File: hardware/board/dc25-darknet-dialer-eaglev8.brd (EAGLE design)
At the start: 101.6 x 101.6 mm, 83 parts, among them SW1 RESET, X1 USB-MICROB, Y1 RESONATORSMD

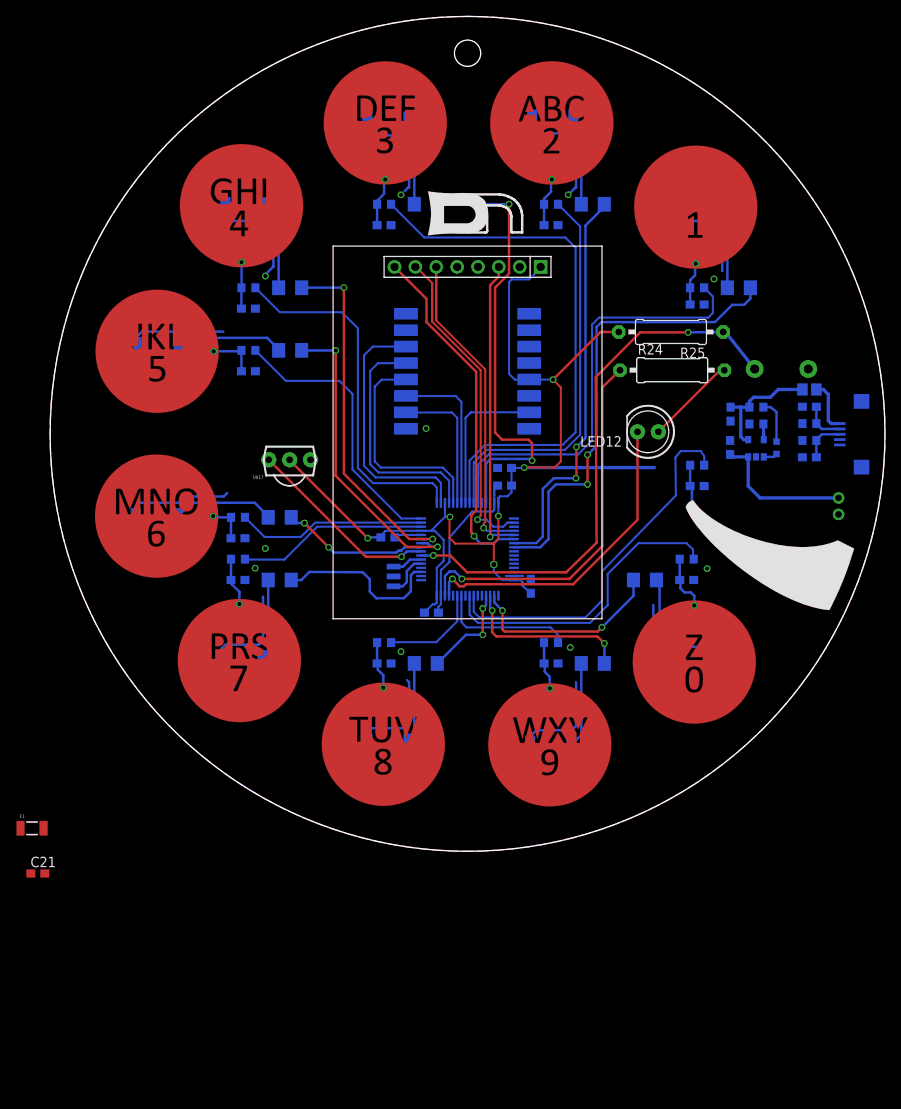
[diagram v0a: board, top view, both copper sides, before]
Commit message: added stlink connector to lbr moved radio spi from spi1 to spi3 to free up pins for touch sensening
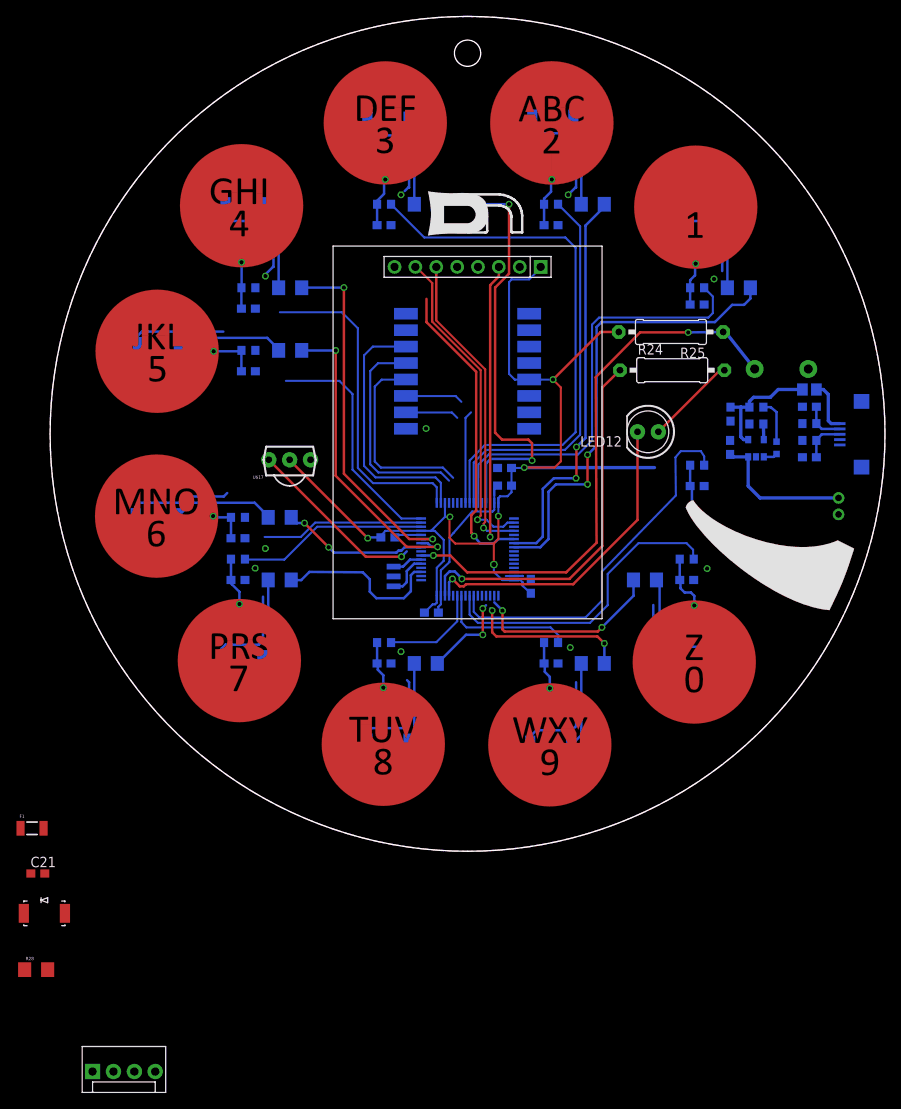
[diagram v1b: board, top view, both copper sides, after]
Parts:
- added LED13: (no value), SYNShop:GULLWING_LED
- added R28: (no value), SYNShop:1206
- added STLINK: STLINK-V2-CONNECTOR, darknet_parts_library:1X04
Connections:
- net N$43 renamed TIM_IR_CARRIER_FREQ
- removed net N$44: U$2.P54
- removed net N$45: U$2.P53
- removed net N$46: U$2.P43
- removed net N$48: U$2.P42
- removed net N$61: U$2.P30
- removed net N$66: U$12.A0
- removed net N$67: U$12.RESET
- removed net OLED_LED: U$12.LED, U$2.P38
- removed net OLED_SPI_MISO: U$2.P35
- new net N$29: LED13.A, R28.2
- new net N$50: U$2.P23
- new net OLED_BACK_LIT: U$12.LED, U$2.P37
- new net OLED_DATA_CMD: U$12.A0, U$2.P35
- new net OLED_RESET: U$12.RESET, U$2.P38
- new net RMF69_INTERRUPT_DIO1: U$15.DIO1, U$2.P30
- new net TSC_G2_I01: R18.1, U$2.P20
- new net TSC_G2_I02: R17.1, U$2.P21
- new net TSC__G2_I03: U$2.P22
- net GND: now also LED13.C, STLINK.GND
- net IR_RCV: now also U$2.P54; no longer U$2.P8
- net LED10: now also U$2.P43; no longer U$2.P50
- net LED8: now also U$2.P8; no longer U$2.P52
- net LED9: now also U$2.P42; no longer U$2.P51
- net LED_STATUS: now also R28.1
- net OLED_CS: no longer U$2.P37
- net RFM69_SPI_MISO: now also U$2.P52; no longer U$2.P22
- net RFM69_SPI_MOSI: now also U$2.P53; no longer U$2.P23
- net RFM69_SPI_NSS: now also U$2.P50; no longer U$2.P20
- net RFM69_SPI_SCK: now also U$2.P51; no longer U$2.P21
- net RMF69_INTERRUPT_DIO0: now also U$15.DIO0; no longer U$15.DIO1
- net SYS_JTCK-SWCLK: now also STLINK.SWDCLK
- net SYS_JTMS_SWDIO: now also STLINK.SWDIO
- net TSC_G1_IO1: now also R16.1; no longer R17.1
- net TSC_G1_IO2: now also R15.1; no longer R16.1
- net TSC_G1_IO3: now also R14.1; no longer R15.1
- net TSC_G1_IO4: no longer R14.1
- net TSC_G5_IO4: no longer R18.1
- net VCC: now also STLINK.VCC
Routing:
- net OLED_LED: track 42.8 -> 0.00 mm, vias 1 -> 0
- net OLED_RESET: track 0.00 -> 37.3 mm, vias 0 -> 1
- net RFM69_SPI_MOSI: track 19.3 -> 7.05 mm
- net RFM69_SPI_MISO: track 16.9 -> 6.53 mm
- net RMF69_INTERRUPT_DIO0: track 18.4 -> 11.3 mm
- net TSC_G1_IO3: track 34.0 -> 28.8 mm
- net TSC_G1_IO4: track 44.0 -> 39.8 mm
- net TSC_G1_IO2: track 23.2 -> 19.8 mm
- net RFM69_SPI_SCK: track 26.7 -> 23.6 mm
- net RFM69_SPI_NSS: track 29.2 -> 26.5 mm
- net OLED_CS: track 36.3 -> 33.6 mm
- net IR_RCV: track 23.7 -> 21.9 mm
- net LED9: track 21.2 -> 19.7 mm
- net LED8: track 11.9 -> 10.7 mm
- net LED10: track 24.3 -> 23.5 mm

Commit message: moved parts onto board, but not in correct location yet
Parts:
- moved STLINK 127.2 mm to (92.3, 70.4), turned to 89.3 degrees
- moved F1 94.9 mm to (84.5, 41.4)
- moved R28 55.5 mm to (31.4, 30.1)
- moved LED13 48.7 mm to (32.4, 27.2)
- moved C21 43.2 mm to (33.9, 22.1)
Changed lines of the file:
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@@
 <element name="L1" library="dp_devices" package="FB603" value="" x="92.4" y="56.2" rot="MR180"/>
 <element name="Y1" library="SparkFun" package="RESONATOR-SMD" value="RESONATORSMD" x="41.8" y="33.45" rot="MR90"/>
-<element name="F1" library="SparkFun" package="PTC-1206" value="500uA" x="-2.2" y="2.8"/>
-<element name="C21" library="SYNShop" package="C0603" value="" x="-1.5" y="-2.7"/>
-<element name="LED13" library="SYNShop" package="GULLWING_LED" value="" x="-3.2" y="-6.05"/>
-<element name="R28" library="SYNShop" package="1206" value="" x="-1.7" y="-14.4"/>
-<element name="STLINK" library="darknet_parts_library" package="1X04" value="STLINK-V2-CONNECTOR" x="10.25" y="-26.8"/>
+<element name="F1" library="SparkFun" package="PTC-1206" value="500uA" x="84.45" y="41.4"/>
+<element name="C21" library="SYNShop" package="C0603" value="" x="33.9" y="22.05"/>
+<element name="LED13" library="SYNShop" package="GULLWING_LED" value="" x="32.4" y="27.2"/>
+<element name="R28" library="SYNShop" package="1206" value="" x="31.4" y="30.15"/>
+<element name="STLINK" library="darknet_parts_library" package="1X04" value="STLINK-V2-CONNECTOR" x="92.35" y="70.4" rot="R89.3"/>
 </elements>
 <signals>
@@
 <wire x1="42.7" y1="79.9" x2="41.49" y2="76.2" width="0" layer="19" extent="16-16"/>
 <wire x1="43.15" y1="80.35" x2="42.7" y2="79.9" width="0" layer="19" extent="16-16"/>
-<wire x1="-2.35" y1="-2.7" x2="20.828" y2="23.344" width="0" layer="19" extent="1-16"/>
-<wire x1="-3.2" y1="-7.55" x2="-2.35" y2="-2.7" width="0" layer="19" extent="1-1"/>
-<wire x1="12.79" y1="-26.8" x2="-3.2" y2="-7.55" width="0" layer="19" extent="1-1"/>
+<wire x1="33.05" y1="22.05" x2="20.828" y2="23.344" width="0" layer="19" extent="1-16"/>
+<wire x1="32.4" y1="25.7" x2="33.05" y2="22.05" width="0" layer="19" extent="1-1"/>
+<wire x1="92.381028125" y1="72.939809375" x2="32.4" y2="25.7" width="0" layer="19" extent="1-1"/>
 </signal>
 <signal name="N$1">
@@
 <contactref element="U$2" pad="P46"/>
 <contactref element="STLINK" pad="SWDIO"/>
-<wire x1="7.71" y1="-26.8" x2="56.45" y2="34" width="0" layer="19" extent="16-16"/>
+<wire x1="92.31896875" y1="67.8601875" x2="56.45" y2="34" width="0" layer="19" extent="16-16"/>
 </signal>
 <signal name="SYS_JTCK-SWCLK">
 <contactref element="U$2" pad="P49"/>
 <contactref element="STLINK" pad="SWDCLK"/>
-<wire x1="10.25" y1="-26.8" x2="54.55" y2="31.1" width="0" layer="19" extent="16-16"/>
+<wire x1="92.35" y1="70.4" x2="54.55" y2="31.1" width="0" layer="19" extent="16-16"/>
 </signal>
 <signal name="TSC_G5_IO1">
@@
 <contactref element="C21" pad="2"/>
 <contactref element="STLINK" pad="VCC"/>
-<wire x1="-0.65" y1="-2.7" x2="45.55" y2="29.05" width="0" layer="19" extent="1-16"/>
-<wire x1="5.17" y1="-26.8" x2="-0.65" y2="-2.7" width="0" layer="19" extent="1-1"/>
+<wire x1="34.75" y1="22.05" x2="45.55" y2="29.05" width="0" layer="19" extent="1-16"/>
+<wire x1="92.2879375" y1="65.320378125" x2="34.75" y2="22.05" width="0" layer="19" extent="1-1"/>
 </signal>
 <signal name="TSC_G3_IO2">
@@
 <contactref element="U$2" pad="P2"/>
 <contactref element="R28" pad="1"/>
-<wire x1="-3.1" y1="-14.4" x2="45.15" y2="33.5" width="0" layer="19" extent="1-16"/>
+<wire x1="30" y1="30.15" x2="45.15" y2="33.5" width="0" layer="19" extent="1-16"/>
 </signal>
 <signal name="TIM_IR_MAIN_SIGNAL">
@@
 <wire x1="84.95" y1="44.45" x2="84.95" y2="48" width="0.4064" layer="16"/>
 <contactref element="F1" pad="1"/>
-<wire x1="-3.6" y1="2.8" x2="82.75" y2="48.3" width="0" layer="19" extent="1-16"/>
+<wire x1="83.05" y1="41.4" x2="82.75" y2="48.3" width="0" layer="19" extent="1-16"/>
 </signal>
 <signal name="N$31">
@@
 <contactref element="LED13" pad="A"/>
 <contactref element="R28" pad="2"/>
-<wire x1="1.8" y1="-7.55" x2="-0.3" y2="-14.4" width="0" layer="19" extent="1-1"/>
+<wire x1="37.4" y1="25.7" x2="32.8" y2="30.15" width="0" layer="19" extent="1-1"/>
 </signal>
 <signal name="TSC_G2_I01">

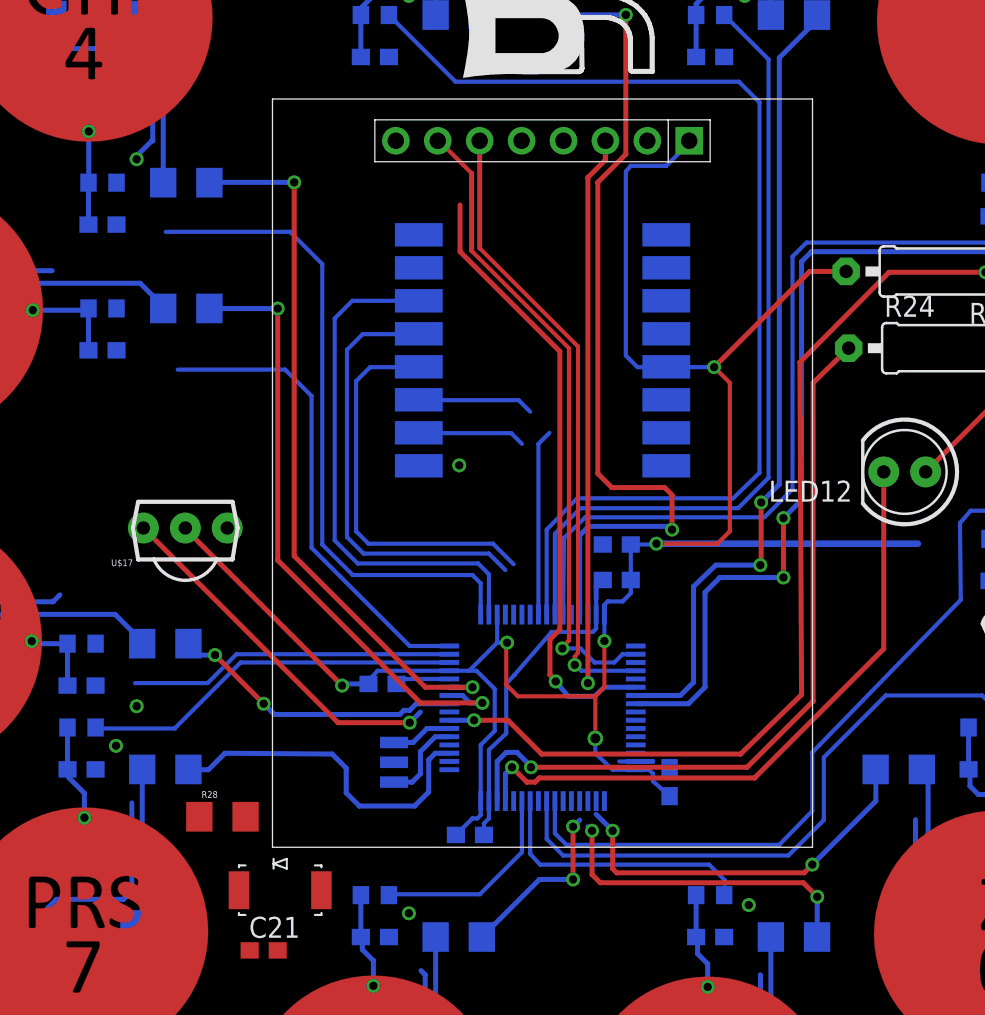
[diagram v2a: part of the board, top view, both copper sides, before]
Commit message: updates to only have 1 pin for IR timer added todo list
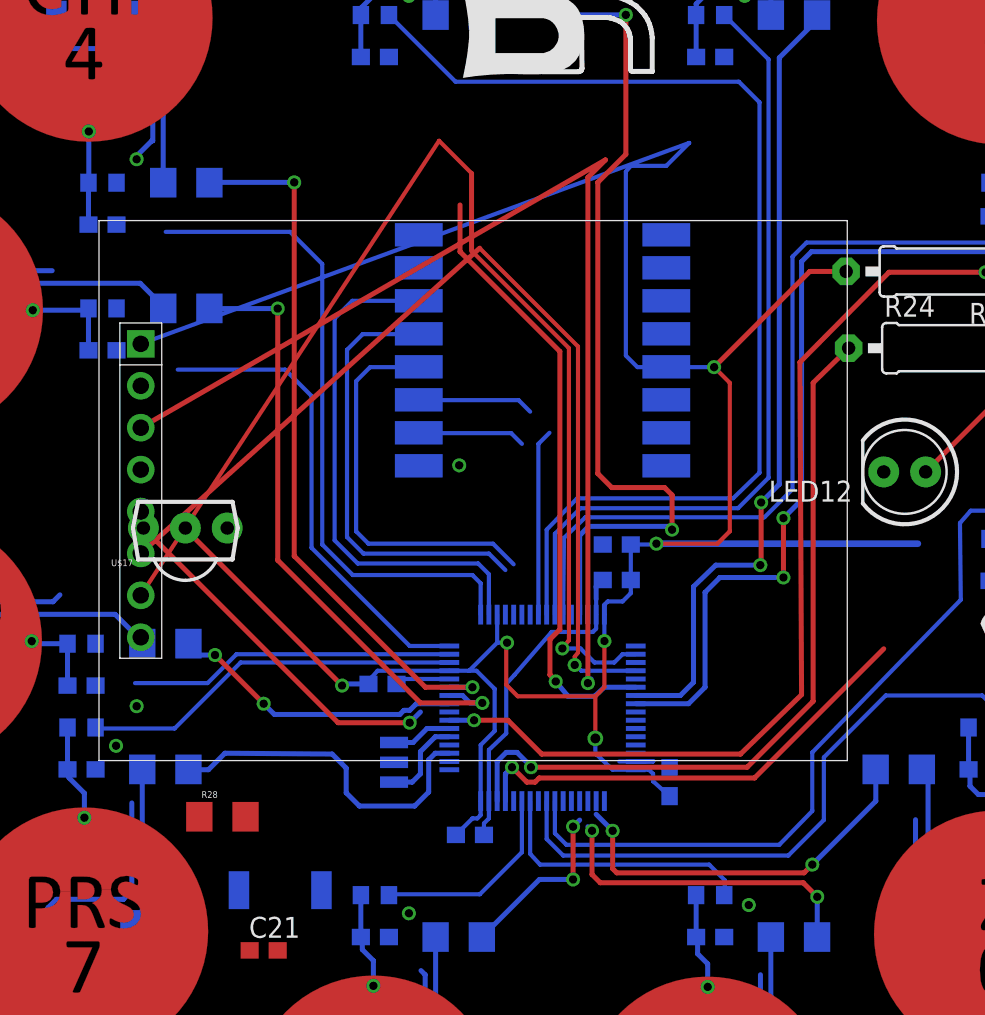
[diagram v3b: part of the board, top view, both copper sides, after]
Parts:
- moved U$12 32.3 mm to (26.4, 49.9), turned to 90 degrees
- moved LED13 5.00 mm to (37.4, 27.2), flipped to the bottom
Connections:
- removed net TIM_IR_MAIN_SIGNAL: LED12.K, U$2.P61
- new net SD_CARD_CS: U$2.P57
- net TIM_IR_CARRIER_FREQ: now also LED12.K, U$2.P61; no longer U$2.P57
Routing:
- net TIM_IR_MAIN_SIGNAL: track 39.2 -> 0.00 mm, vias 1 -> 0
- net VCC: track 130.9 -> 166.2 mm
- net OLED_SPI_SCK: track 39.3 -> 72.1 mm
- net OLED_CS: track 33.6 -> 65.0 mm
- net TIM_IR_CARRIER_FREQ: track 0.00 -> 28.5 mm, vias 0 -> 1
- net OLED_SPI_MOSI: track 38.2 -> 59.3 mm

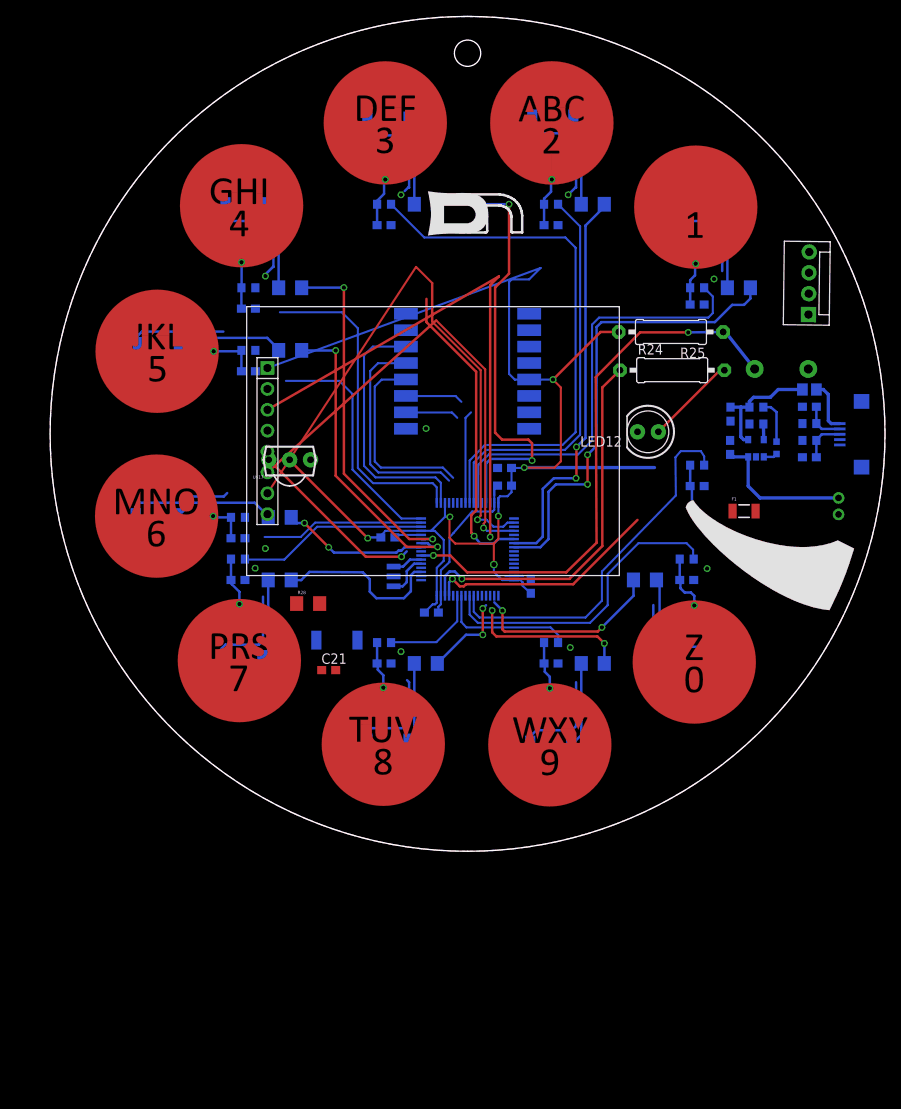
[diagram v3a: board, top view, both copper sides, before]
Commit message: added new part to library: SD_CARD_HEADER diff of todo.txt shows what else was completed on this check in. adding another doc on cap sense and updated stm32cube file
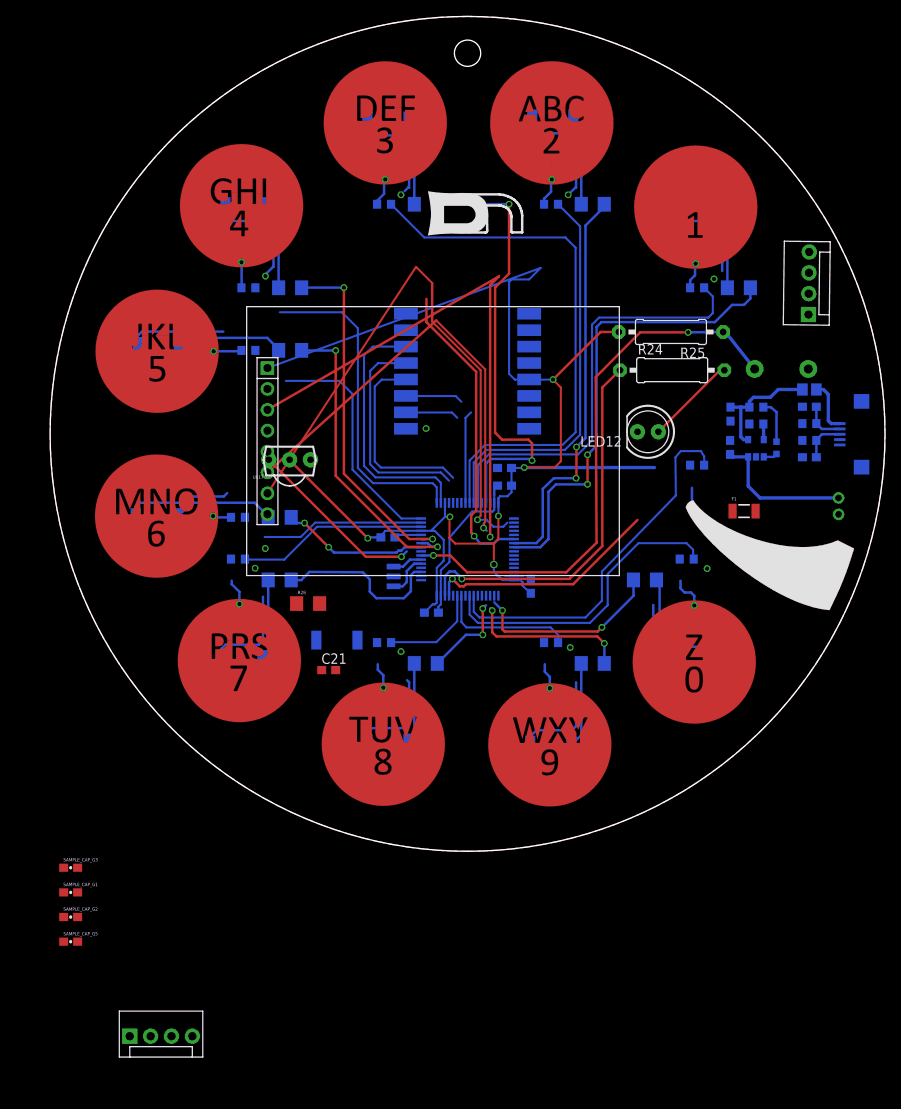
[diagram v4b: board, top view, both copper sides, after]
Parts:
- removed C1, C10, C11, C2, C3, C4, C5, C6, C7, C8, C9: (no value), SYNShop:C0603
- added SAMPLE_CAP_G1, SAMPLE_CAP_G2, SAMPLE_CAP_G3, SAMPLE_CAP_G5: 10pF, SparkFun-Capacitors:0603-CAP
- added SD_CARD_HEADER: SD_CARD_HEADER, darknet_parts_library:SD_CARD_CONNECTOR
- R11, R12, R13, R14, R15, R16, R17, R18, R19, R20, R21: value (none) -> 1K
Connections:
- net OLED_BACK_LIT renamed LCD_BACK_LIT
- net OLED_DATA_CMD renamed LCD_DATA_CMD
- net OLED_RESET renamed LCD_RESET
- net OLED_SPI_MOSI renamed LCD_SPI_MOSI
- net OLED_SPI_SCK renamed LCD_SPI_SCK
- removed net OLED_CS: U$12.CS
- removed net OLED_SPI_NSS: U$2.P33
- removed net SD_CARD_CS: U$2.P57
- removed net TSC__G2_I03: U$2.P22
- new net LCD_SPI_NSS: U$12.CS, U$2.P33
- new net SD_CS: SD_CARD_HEADER.SD_CS, U$2.P57
- new net TSC_G2_I03: SAMPLE_CAP_G2.1, U$2.P22
- net GND: no longer C1.1, C10.1, C11.1, C2.1, C3.1, C4.1, C5.1, C6.1, C7.1, C8.1, C9.1
- net N$1: no longer C1.2
- net N$10: no longer C10.2
- net N$11: no longer C11.2
- net N$2: no longer C2.2
- net N$3: no longer C3.2
- net N$4: no longer C4.2
- net N$5: no longer C5.2
- net N$6: no longer C6.2
- net N$7: no longer C7.2
- net N$8: no longer C8.2
- net N$9: no longer C9.2
- net RFM69_SPI_MISO: now also SD_CARD_HEADER.SD_MISO
- net RFM69_SPI_MOSI: now also SD_CARD_HEADER.SD_MOSI
- net RFM69_SPI_SCK: now also SD_CARD_HEADER.SD_SCK
- net TSC_G1_IO4: now also SAMPLE_CAP_G1.1
- net TSC_G3_IO4: now also SAMPLE_CAP_G3.1
- net TSC_G5_IO4: now also SAMPLE_CAP_G5.1
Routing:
- net OLED_CS: track 65.0 -> 0.00 mm, vias 1 -> 0
- net LCD_SPI_NSS: track 0.00 -> 65.0 mm, vias 0 -> 1
- net LCD_SPI_MOSI: track 59.3 -> 56.0 mm
- net N$11: track 5.22 -> 2.37 mm
- net N$9: track 5.85 -> 3.19 mm
- net N$8: track 5.81 -> 3.15 mm
- net N$7: track 5.89 -> 3.23 mm
- net N$10: track 6.83 -> 4.16 mm
- net N$6: track 4.77 -> 2.23 mm
- net N$5: track 5.96 -> 3.42 mm
- net N$2: track 5.95 -> 3.41 mm
- net N$4: track 5.65 -> 3.11 mm
- net N$3: track 5.98 -> 3.44 mm
- net N$1: track 5.25 -> 3.21 mm
- net LCD_SPI_SCK: track 72.1 -> 71.3 mm
